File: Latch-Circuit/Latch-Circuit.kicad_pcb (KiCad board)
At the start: 2 copper layers, 0 parts

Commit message: 回路図完成、PCBCADに部品追加
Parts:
- added C1: 0.01u, Capacitor_SMD:C_0603_1608Metric, F.Cu at (140.2, 95.6)
- added C10: 0.01u, Capacitor_SMD:C_0603_1608Metric, F.Cu at (140.2, 113.1)
- added C11: 0.01u, Capacitor_SMD:C_0603_1608Metric, F.Cu at (140.2, 115.6)
- added C12: 1000p, Capacitor_SMD:C_1206_3216Metric, F.Cu at (153.1, 125.3)
- added C2: 22u, Capacitor_SMD:C_1206_3216Metric, F.Cu at (153.1, 118.6)
- added C3: 22u, Capacitor_SMD:C_1206_3216Metric, F.Cu at (153.1, 121.9)
- added C4: 0.01u, Capacitor_SMD:C_0603_1608Metric, F.Cu at (140.2, 98.1)
- added C5: 0.01u, Capacitor_SMD:C_0603_1608Metric, F.Cu at (140.2, 100.6)
- added C6: 0.01u, Capacitor_SMD:C_0603_1608Metric, F.Cu at (140.2, 103.1)
- added C7: 0.01u, Capacitor_SMD:C_0603_1608Metric, F.Cu at (140.2, 105.6)
- added C8: 0.01u, Capacitor_SMD:C_0603_1608Metric, F.Cu at (140.2, 108.1)
- added C9: 0.01u, Capacitor_SMD:C_0603_1608Metric, F.Cu at (140.2, 110.6)
- added D1: PZ1AH11B-AU, ProjectEV:D_SOD-123HE_PZ1AHxxxB-AU, F.Cu at (167.3, 126.0)
- added D2: LED, LED_SMD:LED_0603_1608Metric, F.Cu at (166.0, 117.8)
- added D3: LED, LED_SMD:LED_0603_1608Metric, F.Cu at (166.0, 120.4)
- added D4: LED, LED_SMD:LED_0603_1608Metric, F.Cu at (166.0, 123.0)
- added D5: 1N4448WQ-7-F, ProjectEV:D_SOD-123_1N4448W, F.Cu at (161.1, 118.1)
- added D6: 1N4448WQ-7-F, ProjectEV:D_SOD-123_1N4448W, F.Cu at (161.1, 121.3)
- added D7: 1N4448WQ-7-F, ProjectEV:D_SOD-123_1N4448W, F.Cu at (161.1, 124.4)
- added H1: M3, MountingHole:MountingHole_3.2mm_M3_Pad_Via, F.Cu at (134.2, 98.3)
- added H2: M3, MountingHole:MountingHole_3.2mm_M3_Pad_Via, F.Cu at (134.2, 106.2)
- added H3: M3, MountingHole:MountingHole_3.2mm_M3_Pad_Via, F.Cu at (134.2, 114.2)
- added H4: M3, MountingHole:MountingHole_3.2mm_M3_Pad_Via, F.Cu at (134.2, 122.1)
- added J1: SM02B-PASS-1-TB, ProjectEV:Connector_SM02B-PASS-1-TB, F.Cu at (113.7, 75.4)
- added J10: SM02B-PASS-1-TB, ProjectEV:Connector_SM02B-PASS-1-TB, F.Cu at (133.8, 87.5)
- added J2: VH_2pin_Side, ProjectEV:Connector_S2P-VH, F.Cu at (163.7, 78.7)
- added J3: SM02B-PASS-1-TB, ProjectEV:Connector_SM02B-PASS-1-TB, F.Cu at (123.8, 75.4)
- added J4: SM03B-PASS-1-TB, ProjectEV:Connector_SM03B-PASS-1-TB, F.Cu at (144.2, 122.1)
- added J5: SM02B-PASS-1-TB, ProjectEV:Connector_SM02B-PASS-1-TB, F.Cu at (133.8, 75.4)
- added J6: SM02B-PASS-1-TB, ProjectEV:Connector_SM02B-PASS-1-TB, F.Cu at (143.9, 75.4)
- added J7: SM02B-PASS-1-TB, ProjectEV:Connector_SM02B-PASS-1-TB, F.Cu at (153.9, 75.4)
- added J8: SM02B-PASS-1-TB, ProjectEV:Connector_SM02B-PASS-1-TB, F.Cu at (113.7, 87.5)
- added J9: SM02B-PASS-1-TB, ProjectEV:Connector_SM02B-PASS-1-TB, F.Cu at (123.8, 87.5)
- added K1: G5Q-1A4_DC12, ProjectEV:Relay_G5Q-1A4 DC12, F.Cu at (119.5, 100.1)
- added K2: G5Q-1A4_DC12, ProjectEV:Relay_G5Q-1A4 DC12, F.Cu at (119.5, 111.6)
- added K3: G5Q-1A4_DC12, ProjectEV:Relay_G5Q-1A4 DC12, F.Cu at (119.5, 123.2)
- added Q1: 2N7002K-AU, ProjectEV:Package_SOT-23_2N7002K-AU, F.Cu at (160.5, 96.5)
- added Q10: 2N7002K-AU, ProjectEV:Package_SOT-23_2N7002K-AU, F.Cu at (164.9, 114.3)
- added Q11: PJA3439-AU_R1_000A1, ProjectEV:Package_SOT-23_PJA3439-AU_R1_000A1, F.Cu at (169.4, 96.5)
- added Q12: 2N7002K-AU, ProjectEV:Package_SOT-23_2N7002K-AU, F.Cu at (169.4, 101.0)
- added Q13: PJA3439-AU_R1_000A1, ProjectEV:Package_SOT-23_PJA3439-AU_R1_000A1, F.Cu at (169.4, 105.4)
- added Q2: PJA3439-AU_R1_000A1, ProjectEV:Package_SOT-23_PJA3439-AU_R1_000A1, F.Cu at (160.5, 101.0)
- added Q3: DMP3098LQ-7, ProjectEV:Package_SOT-23_DMP3098LQ-7, F.Cu at (160.5, 105.4)
- added Q4: 2N7002K-AU, ProjectEV:Package_SOT-23_2N7002K-AU, F.Cu at (160.5, 109.9)
- added Q5: 2N7002K-AU, ProjectEV:Package_SOT-23_2N7002K-AU, F.Cu at (160.5, 114.3)
- added Q6: PJA3439-AU_R1_000A1, ProjectEV:Package_SOT-23_PJA3439-AU_R1_000A1, F.Cu at (164.9, 96.5)
- added Q7: 2N7002K-AU, ProjectEV:Package_SOT-23_2N7002K-AU, F.Cu at (164.9, 101.0)
- added Q8: PJA3439-AU_R1_000A1, ProjectEV:Package_SOT-23_PJA3439-AU_R1_000A1, F.Cu at (164.9, 105.4)
- added Q9: PJA3439-AU_R1_000A1, ProjectEV:Package_SOT-23_PJA3439-AU_R1_000A1, F.Cu at (164.9, 109.9)
- added R1: 100, Resistor_SMD:R_0603_1608Metric, F.Cu at (144.2, 95.6)
- added R10: 100, Resistor_SMD:R_0603_1608Metric, F.Cu at (148.2, 95.6)
- added R11: 100, Resistor_SMD:R_0603_1608Metric, F.Cu at (148.2, 98.1)
- added R12: 1M, Resistor_SMD:R_0603_1608Metric, F.Cu at (148.2, 100.6)
- added R13: 1M, Resistor_SMD:R_0603_1608Metric, F.Cu at (148.2, 103.1)
- added R14: 100, Resistor_SMD:R_0603_1608Metric, F.Cu at (148.2, 105.6)
- added R15: 1M, Resistor_SMD:R_0603_1608Metric, F.Cu at (148.2, 108.1)
- added R16: 1M, Resistor_SMD:R_0603_1608Metric, F.Cu at (148.2, 110.6)
- added R17: 100, Resistor_SMD:R_0603_1608Metric, F.Cu at (148.2, 113.1)
- added R18: 100, Resistor_SMD:R_0603_1608Metric, F.Cu at (148.2, 115.6)
- added R19: 1M, Resistor_SMD:R_0603_1608Metric, F.Cu at (152.2, 95.6)
- added R2: 1M, Resistor_SMD:R_0603_1608Metric, F.Cu at (144.2, 98.1)
- added R20: 100, Resistor_SMD:R_0603_1608Metric, F.Cu at (152.2, 98.1)
- added R21: 1M, Resistor_SMD:R_0603_1608Metric, F.Cu at (152.2, 100.6)
- added R22: 100, Resistor_SMD:R_0603_1608Metric, F.Cu at (152.2, 103.1)
- added R23: 1M, Resistor_SMD:R_0603_1608Metric, F.Cu at (152.2, 105.6)
- added R24: 1M, Resistor_SMD:R_0603_1608Metric, F.Cu at (152.2, 108.1)
- added R25: 100, Resistor_SMD:R_0603_1608Metric, F.Cu at (152.2, 110.6)
- added R26: 0, Resistor_SMD:R_0603_1608Metric, F.Cu at (152.2, 113.1)
- added R27: 0, Resistor_SMD:R_0603_1608Metric, F.Cu at (152.2, 115.6)
- added R28: 0, Resistor_SMD:R_0603_1608Metric, F.Cu at (156.2, 95.6)
- added R29: 10k, Resistor_SMD:R_0603_1608Metric, F.Cu at (156.2, 98.1)
- added R3: 100, Resistor_SMD:R_0603_1608Metric, F.Cu at (144.2, 100.6)
- added R30: 10k, Resistor_SMD:R_0603_1608Metric, F.Cu at (156.2, 100.6)
- added R31: 10k, Resistor_SMD:R_0603_1608Metric, F.Cu at (156.2, 103.1)
- added R32: 1M, Resistor_SMD:R_1206_3216Metric, F.Cu at (161.7, 88.8)
- added R4: 1M, Resistor_SMD:R_0603_1608Metric, F.Cu at (144.2, 103.1)
- added R5: 100k, Resistor_SMD:R_0603_1608Metric, F.Cu at (144.2, 105.6)
- added R6: 1M, Resistor_SMD:R_0603_1608Metric, F.Cu at (144.2, 108.1)
- added R7: 100, Resistor_SMD:R_0603_1608Metric, F.Cu at (144.2, 110.6)
- added R8: 100, Resistor_SMD:R_0603_1608Metric, F.Cu at (144.2, 113.1)
- added R9: 1M, Resistor_SMD:R_0603_1608Metric, F.Cu at (144.2, 115.6)

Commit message: 若干配置
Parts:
- moved J1 81.3 mm to (195.0, 72.5), turned to -90 degrees
- moved H2 79.5 mm to (195.0, 55.0)
- moved H4 66.6 mm to (195.0, 95.0)
- moved J9 60.7 mm to (175.0, 55.0)
- moved J2 59.3 mm to (105.0, 70.0), turned to -90 degrees
- moved J4 55.7 mm to (105.0, 82.5), turned to 90 degrees
- moved H1 52.2 mm to (105.0, 55.0)
- moved J10 45.0 mm to (165.0, 55.0)
- moved J8 38.8 mm to (135.0, 55.0)
- moved H3 34.9 mm to (105.0, 95.0)
- moved K1 31.1 mm to (127.5, 70.0), turned to 180 degrees
- moved K2 30.2 mm to (127.5, 82.5), turned to 180 degrees
- moved K3 29.3 mm to (127.5, 95.0), turned to 180 degrees
- moved J5 27.8 mm to (115.0, 55.0)
- moved J3 20.5 mm to (125.0, 55.0)
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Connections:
- net Net-(J5-Pin_1) renamed /GLV_IN

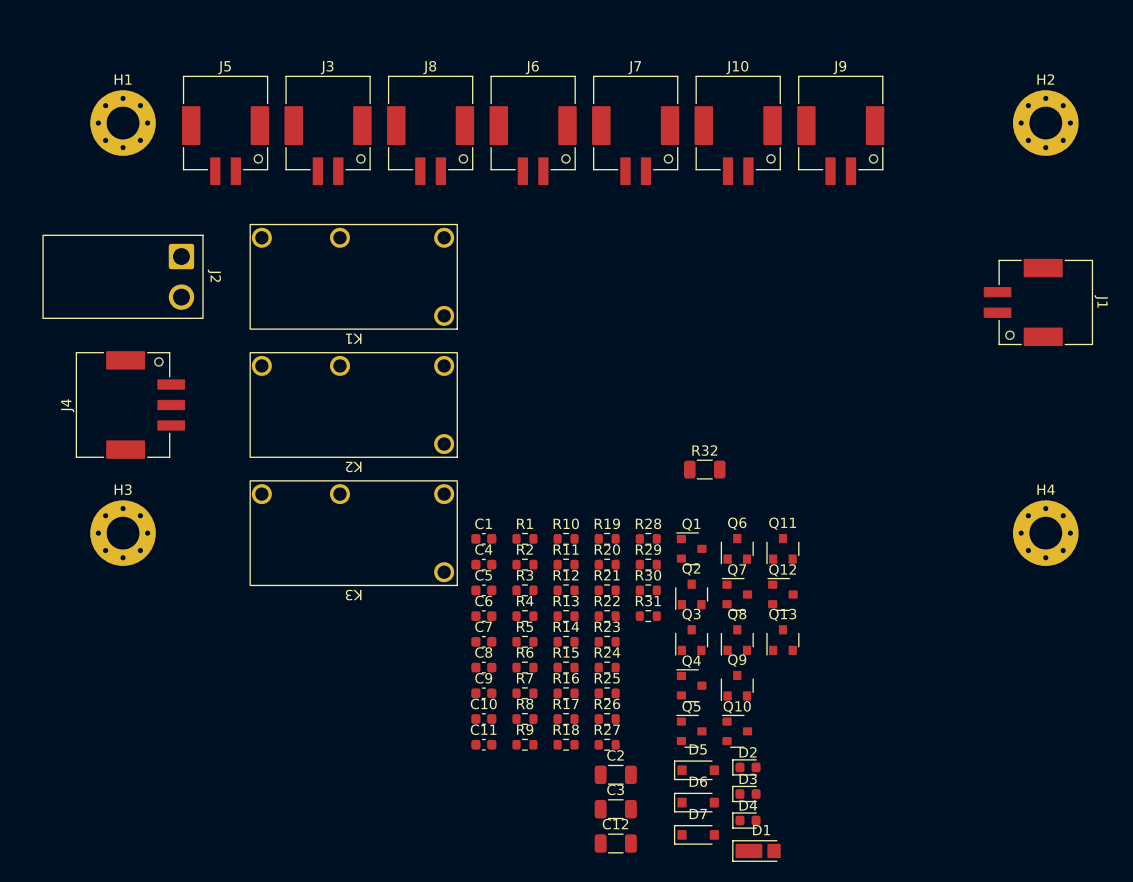
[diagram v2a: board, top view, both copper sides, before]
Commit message: コネクタをトップ型に変更、アノテーション、素子配置
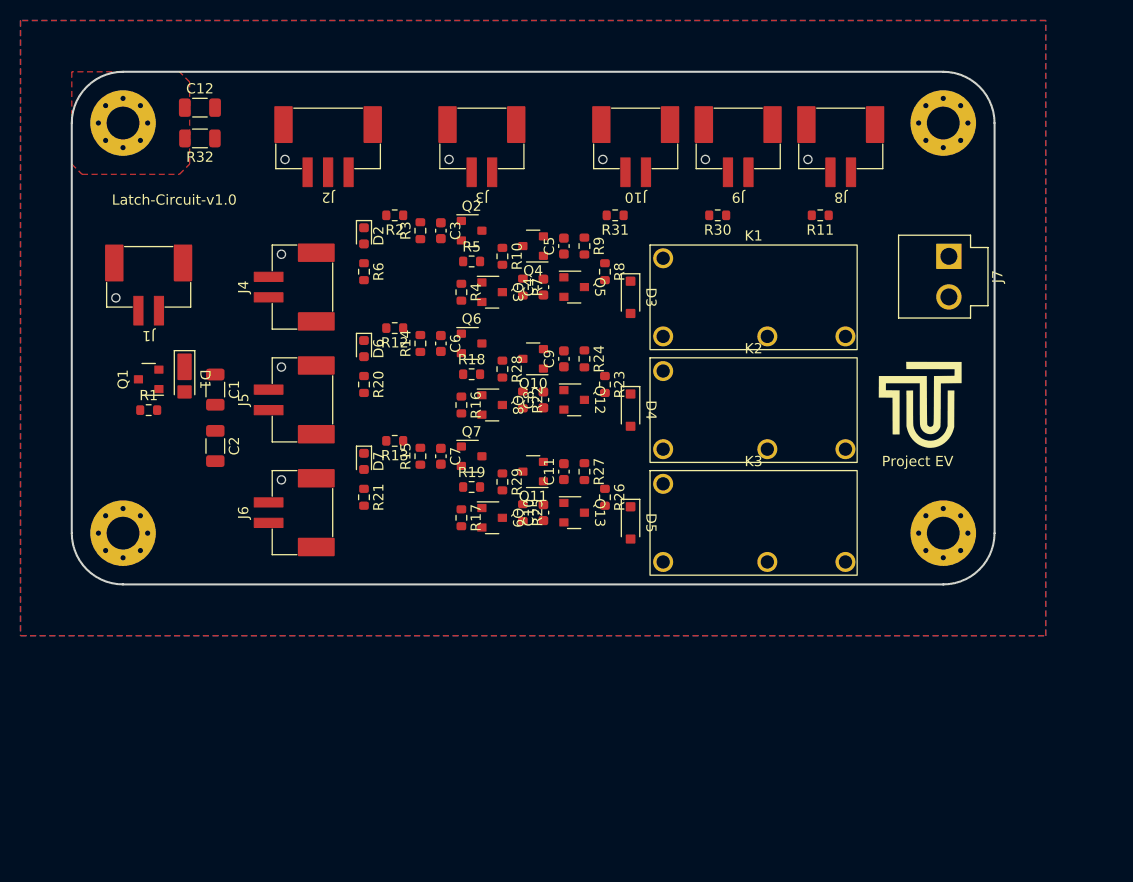
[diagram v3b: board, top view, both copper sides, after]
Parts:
- added G***: Logo_TUT_10x10mm, ProjectEV:Logo_TUT_10x10mm, F.Cu at (182.5, 82.5)
- J1, J10, J3, J5, J6, J8, J9: value SM02B-PASS-1-TB -> BM02B-PASS-1-TF; footprint ProjectEV:Connector_SM02B-PASS-1-TB -> ProjectEV:Connector_BM02B-PASS-1-TF
- J2: value VH_2pin_Side -> BM03B-PASS-1-TF; footprint ProjectEV:Connector_S2P-VH -> ProjectEV:Connector_BM03B-PASS-1-TF
- J4: value SM03B-PASS-1-TB -> BM02B-PASS-1-TF; footprint ProjectEV:Connector_SM03B-PASS-1-TB -> ProjectEV:Connector_BM02B-PASS-1-TF
- J7: value SM02B-PASS-1-TB -> B2P-VH; footprint ProjectEV:Connector_SM02B-PASS-1-TB -> ProjectEV:Connector_B2P-VH
- moved J1 87.5 mm to (107.5, 70.0), turned to 180 degrees
- moved C12 82.4 mm to (112.5, 53.5)
- moved D1 72.7 mm to (111.0, 80.0), turned to -90 degrees
- moved D2 68.2 mm to (128.5, 66.0), turned to -90 degrees
- moved R32 58.9 mm to (112.5, 56.5), turned to 180 degrees
- moved Q1 58.7 mm to (107.5, 80.0), turned to 90 degrees
- moved R11 55.7 mm to (173.0, 64.0), turned to 180 degrees
- moved D6 55.4 mm to (128.5, 77.0), turned to -90 degrees
- moved C1 54.2 mm to (114.0, 81.0), turned to -90 degrees
- moved C2 52.7 mm to (114.0, 86.5), turned to -90 degrees
- moved R30 50.3 mm to (163.0, 64.0), turned to 180 degrees
- moved D7 49.6 mm to (128.5, 88.0), turned to -90 degrees
- moved Q2 49.3 mm to (139.0, 65.5)
- moved D3 46.6 mm to (154.5, 72.0), turned to -90 degrees
- moved Q6 45.9 mm to (139.0, 76.5)
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- renumbered C2 to C1, C6 to C11, C3 to C2, C4 to C3, C11 to C4, C1 to C5, C7 to C6, C5 to C7, C9 to C8, C8 to C9, D4 to D2, D5 to D3, D6 to D4, D7 to D5, D2 to D6, D3 to D7, Q3 to Q1, Q12 to Q10, Q5 to Q11, Q13 to Q12, Q9 to Q13, Q4 to Q2, Q6 to Q3, Q1 to Q4, Q2 to Q5, Q10 to Q6, Q11 to Q8, Q8 to Q9, R5 to R1, R3 to R10, R27 to R11, R18 to R12, R11 to R13, R19 to R14, R12 to R15, R21 to R16, R13 to R17, R20 to R18, R14 to R19, R10 to R2, R29 to R20, R30 to R21, R24 to R22, R22 to R23, R23 to R24, R16 to R25, R8 to R26, R15 to R27, R25 to R28, R17 to R29, R6 to R3, R26 to R30, R28 to R31, R9 to R4, R7 to R5, R31 to R6, R4 to R7, R1 to R8, R2 to R9
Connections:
- J1 pad 1: /BSPD_STATUS -> /GLV_IN
- J2 pad 1: /SHDN_IN -> /AMS_STATUS
- J2 pad 2: /SHDN_OUT -> /IMD_STATUS
- J3 pad 1: /TO_AMS_RST_SW -> /BSPD_STATUS
- J3 pad 2: /AMS_RELAY_DRIVE -> GND
- J4 pad 1: /AMS_STATUS -> /TO_AMS_RST_SW
- J4 pad 2: /IMD_STATUS -> /AMS_RELAY_DRIVE
- J5 pad 1: /GLV_IN -> /TO_BSPD_RST_SW
- J5 pad 2: GND -> /BSPD_RELAY_DRIVE
- J6 pad 1: /TO_BSPD_RST_SW -> /TO_IMD_RST_SW
- J6 pad 2: /BSPD_RELAY_DRIVE -> /IMD_RELAY_DRIVE
- J7 pad 1: /TO_IMD_RST_SW -> /SHDN_IN
- J7 pad 2: /IMD_RELAY_DRIVE -> /SHDN_OUT
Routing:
- added copper zone on B.Cu, net GND
- added copper zone on F.Cu, net GND
- added copper zone on F.Cu, net Net-(C12-Pad1)
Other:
- board outline added: 90 x 50 mm
- board text added: "Latch-Circuit-v1.0"
- board text added: "Project EV"

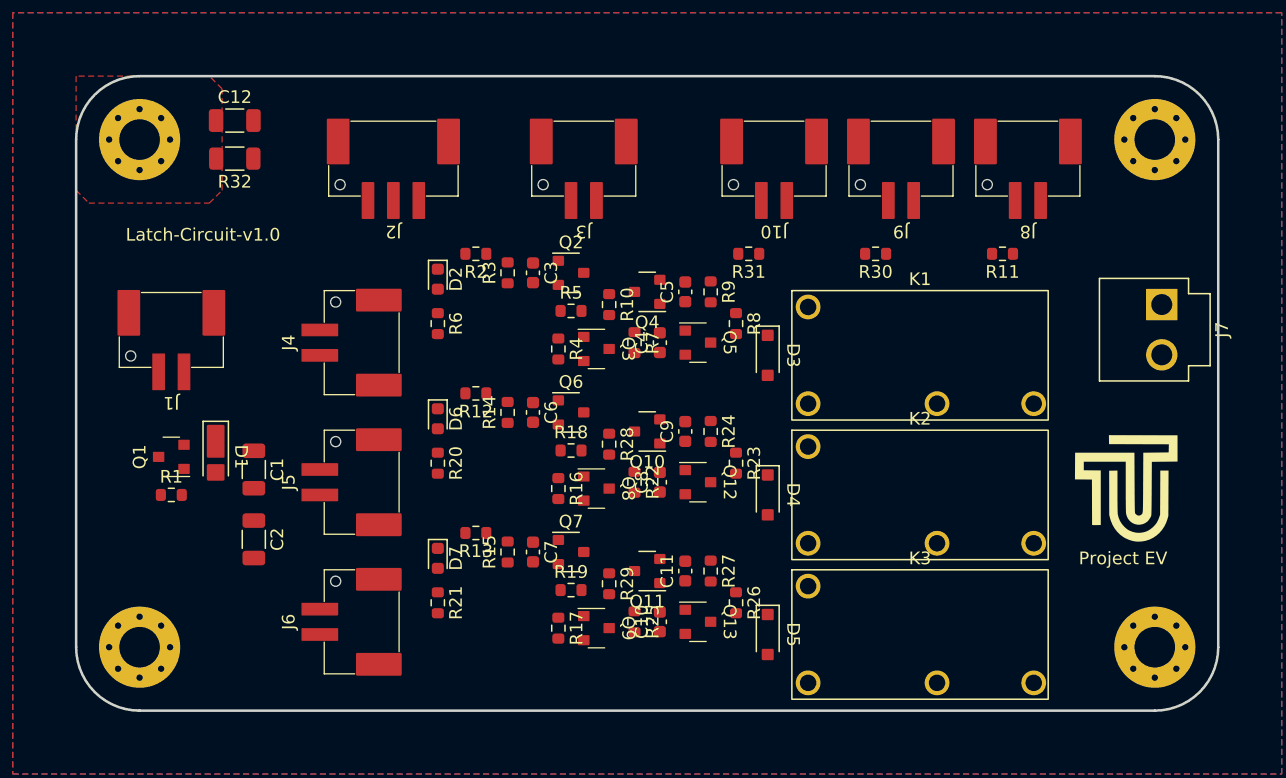
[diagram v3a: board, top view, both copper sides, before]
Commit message: 配線完了、リレー配線修正、外周ビア打ち
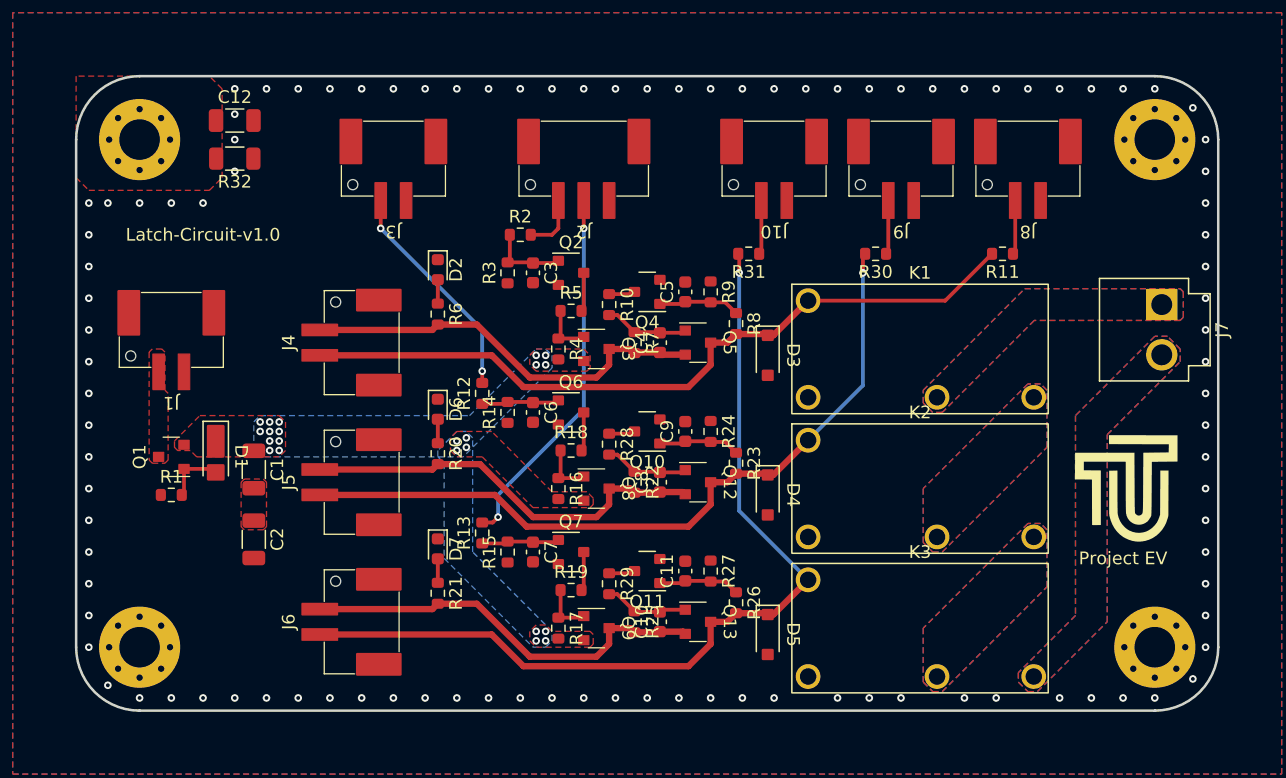
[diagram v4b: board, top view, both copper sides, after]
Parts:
- moved J2 15.0 mm to (140.0, 56.5)
- moved J3 15.0 mm to (125.0, 56.5)
- moved R2 3.81 mm to (135.0, 62.5), turned to 0 degrees
- moved D2 0.75 mm to (128.5, 65.2)
- moved D6 0.75 mm to (128.5, 76.2)
- moved D7 0.75 mm to (128.5, 87.2)
- moved R20 0.75 mm to (128.5, 79.8)
- moved R21 0.75 mm to (128.5, 90.8)
- moved R6 0.75 mm to (128.5, 68.8)
- moved K1 0.50 mm to (166.5, 71.5)
- moved K2 0.50 mm to (166.5, 82.5)
- moved K3 0.50 mm to (166.5, 93.5)
- moved R12 0.50 mm to (132.0, 75.0), turned to 90 degrees
- moved R13 0.50 mm to (132.0, 86.0), turned to 90 degrees
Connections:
- K1 pad 2: Net-(K1-Pad2) -> /SHDN_IN
- K1 pad 3: /SHDN_IN -> Net-(K1-Pad3)
- K2 pad 2: Net-(K2-Pad2) -> Net-(K1-Pad3)
- K2 pad 3: Net-(K1-Pad2) -> Net-(K2-Pad3)
- K3 pad 2: /SHDN_OUT -> Net-(K2-Pad3)
- K3 pad 3: Net-(K2-Pad2) -> /SHDN_OUT
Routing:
- net /IMD_RELAY_DRIVE: track 0.00 -> 71.4 mm, vias 0 -> 1
- net /BSPD_RELAY_DRIVE: track 0.00 -> 60.0 mm, vias 0 -> 1
- net /AMS_RELAY_DRIVE: track 0.00 -> 59.5 mm
- net /TO_BSPD_RST_SW: track 0.00 -> 32.6 mm
- net /TO_IMD_RST_SW: track 0.00 -> 32.6 mm
- net /TO_AMS_RST_SW: track 0.00 -> 32.6 mm
- net /IMD_STATUS: track 0.00 -> 29.2 mm, vias 0 -> 2
- net /BSPD_STATUS: track 0.00 -> 17.7 mm, vias 0 -> 2
- net Net-(Q5-G): track 0.00 -> 6.65 mm
- net Net-(Q13-G): track 0.00 -> 6.65 mm
- net Net-(Q12-G): track 0.00 -> 6.65 mm
- net Net-(Q4-G): track 0.00 -> 6.45 mm
- net Net-(Q11-G): track 0.00 -> 6.45 mm
- net Net-(Q10-G): track 0.00 -> 6.45 mm
- net Net-(Q2-G): track 0.00 -> 6.34 mm
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- added copper zone on B.Cu, net +12V
- added copper zone on F.Cu, net +12V
- added copper zone on F.Cu, net /GLV_IN
- added copper zone on B.Cu, net /SHDN_IN
- added copper zone on F.Cu, net /SHDN_IN
- added copper zone on B.Cu, net /SHDN_OUT
- added copper zone on F.Cu, net /SHDN_OUT
- added copper zone on F.Cu, net Net-(C1-Pad2)
- added copper zone on B.Cu, net Net-(K1-Pad3)
- added copper zone on F.Cu, net Net-(K1-Pad3)
- added copper zone on B.Cu, net Net-(K2-Pad3)
- added copper zone on F.Cu, net Net-(K2-Pad3)

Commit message: 完成
最終チェック後、ガーバー出力
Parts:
- moved R2 1.50 mm to (133.5, 62.5)
- moved C11 0.50 mm to (148.0, 89.5)
- moved C8 0.50 mm to (146.0, 81.5)
- moved R22 0.50 mm to (144.0, 81.5)
- moved R27 0.50 mm to (150.0, 89.5)
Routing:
- net /AMS_STATUS: track 4.58 -> 6.08 mm
- net GND: vias 102 -> 440
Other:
- board text added: "AMS LED"
- board text added: "AMS RST"
- board text added: "AMS/IMD STAT IN"
- board text added: "BSPD LED"
- board text added: "BSPD RST"
- board text added: "BSPD STAT IN"
- board text added: "IMD LED"
- board text added: "IMD RST"
- board text added: "POWER"
- board text added: "SHDN CIRCUIT"
